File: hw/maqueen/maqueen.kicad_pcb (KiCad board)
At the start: 2 copper layers, 80 x 75 mm, 40 parts, among them IC1 MSP430FR2355TPT, J1 conn_DFrobot, J2 ESP01, J3 SBW, SW1 RST, U1 LMV324, Y1 Crystal

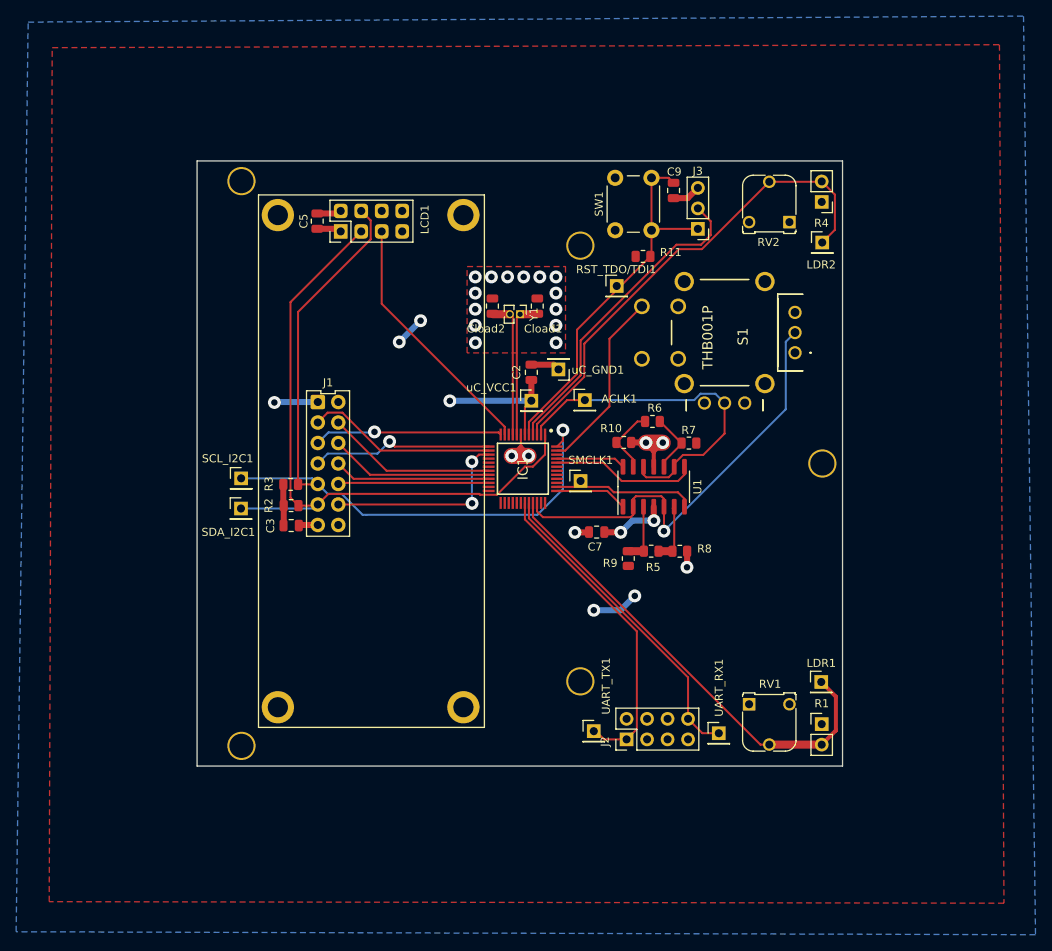
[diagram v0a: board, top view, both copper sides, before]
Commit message: afegit pullupR&debounceC a sel_joystick i noms a silkscreen
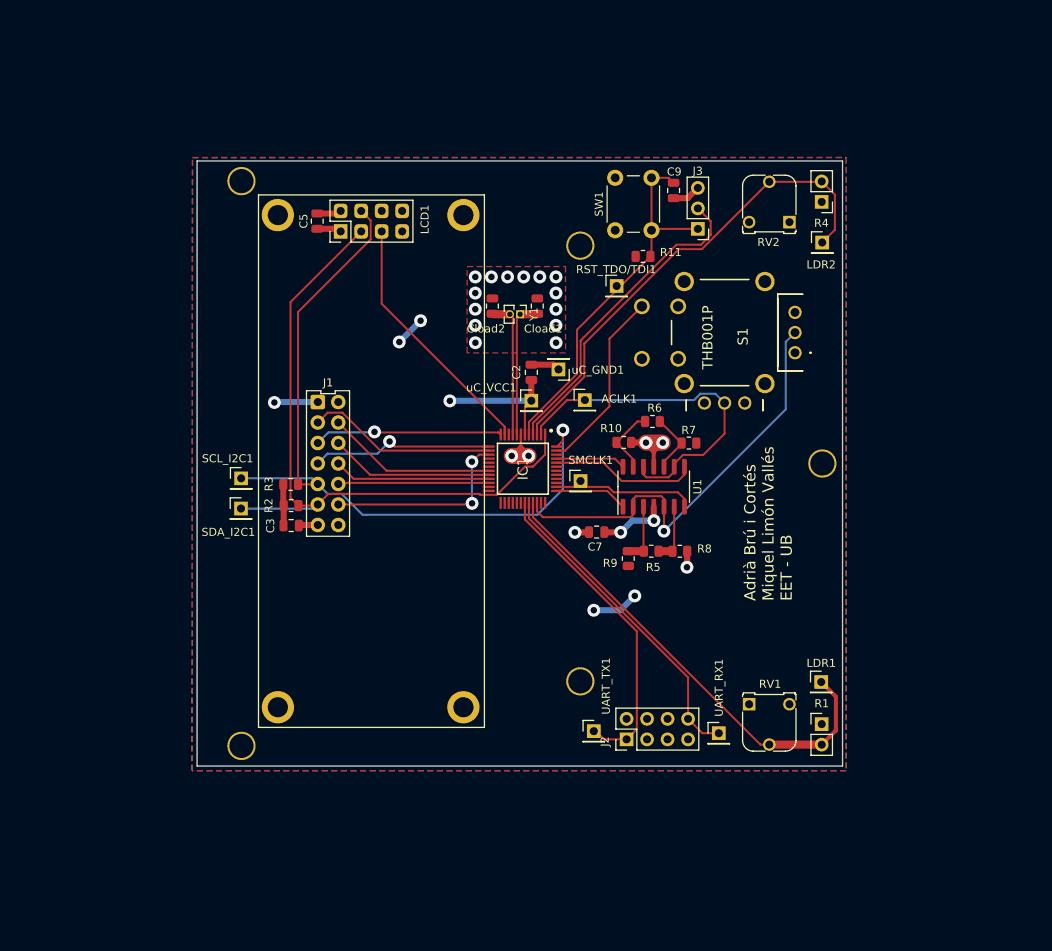
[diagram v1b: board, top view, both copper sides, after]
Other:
- board text added: "Adrià Brú i Cortés Miquel Limón Vallés EET - UB"
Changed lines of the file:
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@@
   (gr_rect locked (start 109.58 62.42) (end 189.58 137.42)
     (stroke (width 0.1) (type default)) (fill none) (layer "Edge.Cuts"))
+  (gr_text "Adrià Brú i Cortés\nMiquel Limón Vallés\nEET - UB" (at 183.46 116.96 90) (layer "F.SilkS")
+    (effects (font (size 1.4 1.4) (thickness 0.15)) (justify left bottom))
+  )
   (dimension (type aligned) (layer "Dwgs.User")
     (pts (xy 117.13 66.63) (xy 117.13 132.63))
@@
     (polygon
       (pts
-        (xy 91.62 48.38)
-        (xy 209.03 48.01)
-        (xy 209.59 154.42)
-        (xy 91.25 154.23)
+        (xy 109.01 62)
+        (xy 190.03 61.99)
+        (xy 190.01 138.01)
+        (xy 108.95 138)
       )
     )
@@
     (polygon
       (pts
-        (xy 88.64 45.21)
-        (xy 212.01 44.47)
-        (xy 213.5 158.33)
-        (xy 87.15 157.96)
+        (xy 109.01 62)
+        (xy 190.03 61.99)
+        (xy 190.02 138)
+        (xy 108.95 138)
       )
     )

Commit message: canvis def disseny
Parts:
- added C1: 100n, Capacitor_SMD:C_0805_2012Metric, F.Cu at (161.5, 87.0)
- added C4: 100n, Capacitor_SMD:C_0805_2012Metric, F.Cu at (162.7, 127.8)
- added D1: LED, LED_THT:LED_D1.8mm_W3.3mm_H2.4mm, F.Cu at (112.5, 92.4)
- added R12: 100, Resistor_SMD:R_0805_2012Metric, F.Cu at (112.5, 88.5)
- added R13: 10k, Resistor_SMD:R_0805_2012Metric, F.Cu at (161.7, 91.3)
- moved R5 1.00 mm to (165.9, 111.8)
- moved R8 1.00 mm to (169.4, 111.8)
- moved R9 1.00 mm to (163.1, 112.7)
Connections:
- IC1 pad 30: unconnected-(IC1-P2.0/TB1.1/COMP0.O-Pad30) -> /WIFI_UART_RX
- J2 pad 6: unconnected-(J2-Pin_6-Pad6) -> /WIFI_UART_RX
- RV1 pad 1: unconnected-(RV1-Pad1) -> PHOTO1
- RV2 pad 1: unconnected-(RV2-Pad1) -> PHOTO2
- S1 pad D1: unconnected-(S1-NO_2-PadD1) -> GND
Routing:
- net GND: track 32.6 -> 38.9 mm, vias 20 -> 22
- net SCL_I2C: track 93.4 -> 97.6 mm
- net +3.3V: track 49.3 -> 53.0 mm
- net Net-(D1-K): track 0.00 -> 3.05 mm
- net LR_JOYSTICK: track 54.8 -> 57.8 mm
- net Net-(U1B--): track 7.62 -> 8.92 mm
- net Net-(U1A-+): track 7.64 -> 8.71 mm

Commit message: placa corregida
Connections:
- IC1 pad 30: /WIFI_UART_RX -> /WIFI_CE
- J2 pad 6: /WIFI_UART_RX -> /WIFI_CE
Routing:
- net /WIFI_CE: track 0.00 -> 34.3 mm
- net /WIFI_UART_TX: track 40.1 -> 50.4 mm
- net PHOTO1: track 58.5 -> 68.6 mm
- net PHOTO2: track 60.3 -> 65.5 mm
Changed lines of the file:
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@@
   (net 58 "unconnected-(IC1-P2.2{slash}TB1CLK-Pad28)")
   (net 59 "unconnected-(IC1-P2.1{slash}TB1.2{slash}COMP1.O-Pad29)")
+  (net 60 "/WIFI_CE")
   (footprint "MiSE:conn_DFrobot" locked (layer "F.Cu")
     (at 127.08 99.92)
@@
     (property "ki_keywords" "connector")
     (attr through_hole)
-    (fp_text reference "J2" (at -0.27 -2.68 90) (layer "F.SilkS")
+    (fp_text reference "J2" (at 1.112 -6.514 90) (layer "F.SilkS")
         (effects (font (size 1 1) (thickness 0.15)))
     )
@@
       (net 26 "unconnected-(J2-Pin_5-Pad5)") (pinfunction "Pin_5") (pintype "passive+no_connect"))
     (pad "6" thru_hole oval (at 2.54 5.08 90) (size 1.7 1.7) (drill 1) (layers "*.Cu" "*.Mask")
-      (net 8 "/WIFI_UART_RX") (pinfunction "Pin_6") (pintype "passive"))
+      (net 60 "/WIFI_CE") (pinfunction "Pin_6") (pintype "passive"))
     (pad "7" thru_hole oval (at 0 7.62 90) (size 1.7 1.7) (drill 1) (layers "*.Cu" "*.Mask")
       (net 3 "GND") (pinfunction "Pin_7") (pintype "passive"))
@@
         (effects (font (size 1 1) (thickness 0.15)))
     )
-    (fp_text user "${REFERENCE}" (at 0 0 90) (layer "F.Fab")
+    (fp_text user "${REFERENCE}" (at -3.95 -0.196 90) (layer "F.Fab")
         (effects (font (size 1 1) (thickness 0.15)))
     )
@@
       (net 59 "unconnected-(IC1-P2.1{slash}TB1.2{slash}COMP1.O-Pad29)") (pinfunction "P2.1/TB1.2/COMP1.O") (pintype "passive+no_connect"))
     (pad "30" smd rect (at 4.238 0.25) (size 0.3 1.475) (layers "F.Cu" "F.Paste" "F.Mask")
-      (net 8 "/WIFI_UART_RX") (pinfunction "P2.0/TB1.1/COMP0.O") (pintype "passive"))
+      (net 60 "/WIFI_CE") (pinfunction "P2.0/TB1.1/COMP0.O") (pintype "passive"))
     (pad "31" smd rect (at 4.238 -0.25) (size 0.3 1.475) (layers "F.Cu" "F.Paste" "F.Mask")
       (net 9 "/WIFI_UART_TX") (pinfunction "P1.7/UCA0TXD/UCA0SIMO/TB0.2/TDO/OA1+/A7/VREF+") (pintype "passive"))
@@
   (via (at 166.035 108.44) (size 1.6) (drill 0.8) (layers "F.Cu" "B.Cu") (net 2))
   (via (at 163.83 116.332) (size 1.6) (drill 0.8) (layers "F.Cu" "B.Cu") (net 2))
-  (via (at 158.75 118.11) (size 1.6) (drill 0.8) (layers "F.Cu" "B.Cu") (free) (net 2))
+  (via (at 158.3 118.1) (size 1.6) (drill 0.8) (layers "F.Cu" "B.Cu") (free) (net 2))
   (via (at 140.91 92.16) (size 1.6) (drill 0.8) (layers "F.Cu" "B.Cu") (net 2))
   (via (at 119.16 92.36) (size 1.6) (drill 0.8) (layers "F.Cu" "B.Cu") (net 2))
   (via (at 134.64 84.86) (size 1.6) (drill 0.8) (layers "F.Cu" "B.Cu") (free) (net 2))
+  (segment (start 158.3 118.1) (end 158.31 118.11) (width 0.75) (layer "B.Cu") (net 2))
   (segment (start 166.035 108.44) (end 162.1 108.44) (width 0.75) (layer "B.Cu") (net 2))
-  (segment (start 162.052 118.11) (end 163.83 116.332) (width 0.75) (layer "B.Cu") (net 2))
   (segment (start 119.22 92.3) (end 119.16 92.36) (width 0.75) (layer "B.Cu") (net 2))
   (segment (start 134.64 84.86) (end 137.28 82.22) (width 0.75) (layer "B.Cu") (net 2))
   (segment (start 124.54 92.3) (end 119.22 92.3) (width 0.75) (layer "B.Cu") (net 2))
+  (segment (start 162.052 118.11) (end 163.83 116.332) (width 0.75) (layer "B.Cu") (net 2))
   (segment (start 151.01 92.14) (end 140.93 92.14) (width 0.75) (layer "B.Cu") (net 2))
+  (segment (start 158.31 118.11) (end 162.052 118.11) (width 0.75) (layer "B.Cu") (net 2))
   (segment (start 162.1 108.44) (end 162.09 108.45) (width 0.75) (layer "B.Cu") (net 2))
   (segment (start 140.93 92.14) (end 140.91 92.16) (width 0.75) (layer "B.Cu") (net 2))
-  (segment (start 158.75 118.11) (end 162.052 118.11) (width 0.75) (layer "B.Cu") (net 2))
   (segment (start 112.47 85.58) (end 112.43 85.54) (width 0.75) (layer "F.Cu") (net 3))
   (segment (start 127.065 68.93) (end 127.38 68.615) (width 0.75) (layer "F.Cu") (net 3))
@@
   (segment (start 156.44 108.49) (end 156.41 108.46) (width 0.75) (layer "F.Cu") (net 3))
   (segment (start 150.66 98.79) (end 149.7 97.83) (width 0.5) (layer "F.Cu") (net 3))
-  (segment (start 149.73 97.8) (end 149.7 97.83) (width 0.25) (layer "F.Cu") (net 3))
   (segment (start 151.01 87.67) (end 153.78 87.67) (width 0.75) (layer "F.Cu") (net 3))
   (segment (start 168.64 67.03) (end 170.38 67.03) (width 0.75) (layer "F.Cu") (net 3))
@@
   (segment (start 170.434 131.572) (end 170.434 126.433482) (width 0.25) (layer "F.Cu") (net 8))
   (segment (start 150.71 106.709482) (end 150.71 104.808) (width 0.25) (layer "F.Cu") (net 8))
+  (segment (start 162.814 134.112) (end 162.814 134.814) (width 0.25) (layer "F.Cu") (net 9))
+  (segment (start 163.8 135.8) (end 168.5 135.8) (width 0.25) (layer "F.Cu") (net 9))
+  (segment (start 162.814 134.814) (end 163.8 135.8) (width 0.25) (layer "F.Cu") (net 9))
   (segment (start 159.004 133.096) (end 160.02 134.112) (width 0.25) (layer "F.Cu") (net 9))
   (segment (start 158.75 133.096) (end 159.004 133.096) (width 0.25) (layer "F.Cu") (net 9))
-  (segment (start 162.814 134.112) (end 164.084 132.842) (width 0.25) (layer "F.Cu") (net 9))
-  (segment (start 160.02 134.112) (end 162.814 134.112) (width 0.25) (layer "F.Cu") (net 9))
-  (segment (start 164.084 120.719878) (end 150.21 106.845878) (width 0.25) (layer "F.Cu") (net 9))
+  (segment (start 169.132061 125.767939) (end 150.21 106.845878) (width 0.25) (layer "F.Cu") (net 9))
+  (segment (start 169.132061 135.167939) (end 169.132061 125.767939) (width 0.25) (layer "F.Cu") (net 9))
   (segment (start 150.21 106.845878) (end 150.21 104.808) (width 0.25) (layer "F.Cu") (net 9))
-  (segment (start 164.084 132.842) (end 164.084 120.719878) (width 0.25) (layer "F.Cu") (net 9))
+  (segment (start 160.02 134.112) (end 162.814 134.112) (width 0.25) (layer "F.Cu") (net 9))
+  (segment (start 168.5 135.8) (end 169.132061 135.167939) (width 0.25) (layer "F.Cu") (net 9))
   (segment (start 145.722 100.82) (end 133.06 100.82) (width 0.25) (layer "F.Cu") (net 10))
   (segment (start 133.06 100.82) (end 127.08 94.84) (width 0.25) (layer "F.Cu") (net 10))
@@
   (segment (start 147.71 95.37) (end 147.71 96.332) (width 0.25) (layer "F.Cu") (net 38))
   (segment (start 169.29 73.35) (end 172.15 73.35) (width 0.25) (layer "F.Cu") (net 39))
+  (segment (start 183 70) (end 184.53 70) (width 0.5) (layer "F.Cu") (net 39))
   (segment (start 180.5 65) (end 186.96 65) (width 0.25) (layer "F.Cu") (net 39))
   (segment (start 151.71 96.332) (end 151.71 95.042792) (width 0.25) (layer "F.Cu") (net 39))
   (segment (start 157.57 85.07) (end 169.29 73.35) (width 0.25) (layer "F.Cu") (net 39))
+  (segment (start 184.53 70) (end 187.06 72.53) (width 0.5) (layer "F.Cu") (net 39))
   (segment (start 188.63 70.96) (end 188.63 66.59) (width 0.25) (layer "F.Cu") (net 39))
   (segment (start 151.71 95.042792) (end 157.57 89.182792) (width 0.25) (layer "F.Cu") (net 39))
@@
   (segment (start 151.21 104.808) (end 151.21 106.573086) (width 0.25) (layer "F.Cu") (net 40))
   (segment (start 180.505 134.765) (end 180.5 134.76) (width 0.25) (layer "F.Cu") (net 40))
+  (segment (start 178 129.76) (end 180.76 127) (width 0.5) (layer "F.Cu") (net 40))
   (segment (start 179.401914 134.765) (end 180.505 134.765) (width 0.25) (layer "F.Cu") (net 40))
   (segment (start 151.21 106.573086) (end 179.401914 134.765) (width 0.25) (layer "F.Cu") (net 40))
   (segment (start 187 134.765) (end 180.505 134.765) (width 1) (layer "F.Cu") (net 40))
   (segment (start 188.76 133.005) (end 187 134.765) (width 0.5) (layer "F.Cu") (net 40))
+  (segment (start 180.76 127) (end 186.94 127) (width 0.5) (layer "F.Cu") (net 40))
+  (segment (start 149.71 106.982274) (end 149.71 104.808) (width 0.25) (layer "F.Cu") (net 60))
+  (segment (start 167.894 125.166274) (end 149.71 106.982274) (width 0.25) (layer "F.Cu") (net 60))
+  (segment (start 167.894 131.572) (end 167.894 125.166274) (width 0.25) (layer "F.Cu") (net 60))
   (zone (net 3) (net_name "GND") (layer "F.Cu") (hatch edge 0.5)
     (priority 2)

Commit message: maqueeeeeeeeeeeeeen
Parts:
- added G***: LOGO, maqueen_pics:maqueen2, F.Cu at (137.8, 120.4)
- added G***: LOGO, maqueen_pics:maqueen5, F.Cu at (180.1, 113.0)
- added G***: LOGO, maqueen_pics:maqueen3, F.Cu at (132.3, 83.2)
- added G***: LOGO, maqueen_pics:maqueen1, F.Cu at (126.0, 118.6)
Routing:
- net L_JOYSTICK: track 8.98 -> 9.51 mm
